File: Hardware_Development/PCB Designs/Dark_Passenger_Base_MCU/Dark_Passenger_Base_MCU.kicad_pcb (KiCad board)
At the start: 2 copper layers, 87.5 x 64.9 mm, 28 parts, among them J1 Conn_01x22, J10 SPARE I2C, J11 IMU, J12 Toggle Switches, J13 Spare, J14 Motor Encoder 1, J15 Motor Encoder 2, J16 RESET, J18 Motor Control, J2 Conn_01x22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

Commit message: Updates to Base PCB
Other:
- board text added: "Dark Passenger Base MCU REV: 1.0 Name: Ranil Ganlath Date: 03-28-2025 S/N:"
- board text removed: "Dark Passenger Base MCU REV: 1.0 Name: Ranil Ganlath Date: 03-27-2025 S/N:"
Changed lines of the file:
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@@
 	(title_block
 		(title "Dark Passenger Base MCU PCB")
-		(date "2025-03-27")
+		(date "2025-03-28")
 		(rev "1.0")
 		(company "Ranil Ganlath")
@@
 			(at -3.5558 -0.0508 0)
 			(layer "F.SilkS")
+			(hide yes)
 			(effects
 				(font
@@
 			(at -3.5558 0 0)
 			(layer "F.SilkS")
+			(hide yes)
 			(effects
 				(font
@@
 		)
 	)
+	(gr_text "5V"
+		(at 122.098 82.6516 90)
+		(layer "F.SilkS")
+		(effects
+			(font
+				(size 1 1)
+				(thickness 0.2)
+			)
+			(justify left bottom)
+		)
+	)
 	(gr_text "3V"
 		(at 85.892 54.6676 0)
@@
 		)
 	)
-	(gr_text "Dark Passenger \nBase MCU\nREV: 1.0\nName: Ranil Ganlath\nDate: 03-27-2025\n\nS/N:"
+	(gr_text "Dark Passenger \nBase MCU\nREV: 1.0\nName: Ranil Ganlath\nDate: 03-28-2025\n\nS/N:"
 		(at 100.508 94.58 0)
 		(layer "F.SilkS")
@@
 		)
 	)
+	(gr_text "GND"
+		(at 124.7904 83.7184 90)
+		(layer "F.SilkS")
+		(effects
+			(font
+				(size 1 1)
+				(thickness 0.2)
+			)
+			(justify left bottom)
+		)
+	)
 	(gr_text "Motor Encoder 3 / 4"
 		(at 97.5108 62.738 90)
@@
 	)
 	(gr_text "RST"
-		(at 113.462 63.5 0)
+		(at 113.208 66.294 0)
 		(layer "B.SilkS")
 		(effects
@@
 	)
 	(gr_text "GND"
-		(at 113.462 66.294 0)
+		(at 113.4112 63.5 0)
 		(layer "B.SilkS")
 		(effects
@@
 			)
 		)
+	)
+	(zone
+		(net 0)
+		(net_name "")
+		(layers "F.Cu" "B.Cu")
+		(hatch edge 0.5)
+		(connect_pads
+			(clearance 0)
+		)
+		(min_thickness 0.25)
+		(filled_areas_thickness no)
+		(keepout
+			(tracks allowed)
+			(vias allowed)
+			(pads allowed)
+			(copperpour not_allowed)
+			(footprints allowed)
+		)
+		(placement
+			(enabled no)
+			(sheetname "")
+		)
+		(fill
+			(thermal_gap 0.5)
+			(thermal_bridge_width 0.5)
+		)
+		(polygon
+			(pts
+				(xy 92.798023 91.137979) (xy 92.766261 90.815496) (xy 92.703043 90.497679) (xy 92.608979 90.18759)
+				(xy 92.484973 89.888213) (xy 92.33222 89.602433) (xy 92.152191 89.333001) (xy 91.946621 89.082512)
+				(xy 91.717488 88.853379) (xy 91.466999 88.647809) (xy 91.197567 88.46778) (xy 90.911787 88.315027)
+				(xy 90.61241 88.191021) (xy 90.302321 88.096957) (xy 89.984504 88.033739) (xy 89.662021 88.001977)
+				(xy 89.337979 88.001977) (xy 89.015496 88.033739) (xy 88.697679 88.096957) (xy 88.38759 88.191021)
+				(xy 88.088213 88.315027) (xy 87.802433 88.46778) (xy 87.533001 88.647809) (xy 87.282512 88.853379)
+				(xy 87.053379 89.082512) (xy 86.847809 89.333001) (xy 86.66778 89.602433) (xy 86.515027 89.888213)
+				(xy 86.391021 90.18759) (xy 86.296957 90.497679) (xy 86.233739 90.815496) (xy 86.201977 91.137979)
+				(xy 86.201977 91.462021) (xy 86.233739 91.784504) (xy 86.296957 92.102321) (xy 86.391021 92.41241)
+				(xy 86.515027 92.711787) (xy 86.66778 92.997567) (xy 86.847809 93.266999) (xy 87.053379 93.517488)
+				(xy 87.282512 93.746621) (xy 87.533001 93.952191) (xy 87.802433 94.13222) (xy 88.088213 94.284973)
+				(xy 88.38759 94.408979) (xy 88.697679 94.503043) (xy 89.015496 94.566261) (xy 89.337979 94.598023)
+				(xy 89.662021 94.598023) (xy 89.984504 94.566261) (xy 90.302321 94.503043) (xy 90.61241 94.408979)
+				(xy 90.911787 94.284973) (xy 91.197567 94.13222) (xy 91.466999 93.952191) (xy 91.717488 93.746621)
+				(xy 91.946621 93.517488) (xy 92.152191 93.266999) (xy 92.33222 92.997567) (xy 92.484973 92.711787)
+				(xy 92.608979 92.41241) (xy 92.703043 92.102321) (xy 92.766261 91.784504) (xy 92.798023 91.462021)
+			)
+		)
+	)
+	(zone
+		(net 0)
+		(net_name "")
+		(layers "F.Cu" "B.Cu")
+		(hatch edge 0.5)
+		(connect_pads
+			(clearance 0)
+		)
+		(min_thickness 0.25)
+		(filled_areas_thickness no)
+		(keepout
+			(tracks allowed)
+			(vias allowed)
+			(pads allowed)
+			(copperpour not_allowed)
+			(footprints allowed)
+		)
+		(placement
+			(enabled no)
+			(sheetname "")
+		)
+		(fill
+			(thermal_gap 0.5)
+			(thermal_bridge_width 0.5)
+		)
+		(polygon
+			(pts
+				(xy 171.538023 91.137979) (xy 171.506261 90.815496) (xy 171.443043 90.497679) (xy 171.348979 90.18759)
+				(xy 171.224973 89.888213) (xy 171.07222 89.602433) (xy 170.892191 89.333001) (xy 170.686621 89.082512)
+				(xy 170.457488 88.853379) (xy 170.206999 88.647809) (xy 169.937567 88.46778) (xy 169.651787 88.315027)
+				(xy 169.35241 88.191021) (xy 169.042321 88.096957) (xy 168.724504 88.033739) (xy 168.402021 88.001977)
+				(xy 168.077979 88.001977) (xy 167.755496 88.033739) (xy 167.437679 88.096957) (xy 167.12759 88.191021)
+				(xy 166.828213 88.315027) (xy 166.542433 88.46778) (xy 166.273001 88.647809) (xy 166.022512 88.853379)
+				(xy 165.793379 89.082512) (xy 165.587809 89.333001) (xy 165.40778 89.602433) (xy 165.255027 89.888213)
+				(xy 165.131021 90.18759) (xy 165.036957 90.497679) (xy 164.973739 90.815496) (xy 164.941977 91.137979)
+				(xy 164.941977 91.462021) (xy 164.973739 91.784504) (xy 165.036957 92.102321) (xy 165.131021 92.41241)
+				(xy 165.255027 92.711787) (xy 165.40778 92.997567) (xy 165.587809 93.266999) (xy 165.793379 93.517488)
+				(xy 166.022512 93.746621) (xy 166.273001 93.952191) (xy 166.542433 94.13222) (xy 166.828213 94.284973)
+				(xy 167.12759 94.408979) (xy 167.437679 94.503043) (xy 167.755496 94.566261) (xy 168.077979 94.598023)
+				(xy 168.402021 94.598023) (xy 168.724504 94.566261) (xy 169.042321 94.503043) (xy 169.35241 94.408979)
+				(xy 169.651787 94.284973) (xy 169.937567 94.13222) (xy 170.206999 93.952191) (xy 170.457488 93.746621)
+				(xy 170.686621 93.517488) (xy 170.892191 93.266999) (xy 171.07222 92.997567) (xy 171.224973 92.711787)
+				(xy 171.348979 92.41241) (xy 171.443043 92.102321) (xy 171.506261 91.784504) (xy 171.538023 91.462021)
+			)
+		)
+	)
+	(zone
+		(net 0)
+		(net_name "")
+		(layers "F.Cu" "B.Cu")
+		(hatch edge 0.5)
+		(connect_pads
+			(clearance 0)
+		)
+		(min_thickness 0.25)
+		(filled_areas_thickness no)
+		(keepout
+			(tracks allowed)
+			(vias allowed)
+			(pads allowed)
+			(copperpour not_allowed)
+			(footprints allowed)
+		)
+		(placement
+			(enabled no)
+			(sheetname "")
+		)
+		(fill
+			(thermal_gap 0.5)
+			(thermal_bridge_width 0.5)
+		)
+		(polygon
+			(pts
+				(xy 171.547823 35.245579) (xy 171.516061 34.923096) (xy 171.452843 34.605279) (xy 171.358779 34.29519)
+				(xy 171.234773 33.995813) (xy 171.08202 33.710033) (xy 170.901991 33.440601) (xy 170.696421 33.190112)
+				(xy 170.467288 32.960979) (xy 170.216799 32.755409) (xy 169.947367 32.57538) (xy 169.661587 32.422627)
+				(xy 169.36221 32.298621) (xy 169.052121 32.204557) (xy 168.734304 32.141339) (xy 168.411821 32.109577)
+				(xy 168.087779 32.109577) (xy 167.765296 32.141339) (xy 167.447479 32.204557) (xy 167.13739 32.298621)
+				(xy 166.838013 32.422627) (xy 166.552233 32.57538) (xy 166.282801 32.755409) (xy 166.032312 32.960979)
+				(xy 165.803179 33.190112) (xy 165.597609 33.440601) (xy 165.41758 33.710033) (xy 165.264827 33.995813)
+				(xy 165.140821 34.29519) (xy 165.046757 34.605279) (xy 164.983539 34.923096) (xy 164.951777 35.245579)
+				(xy 164.951777 35.569621) (xy 164.983539 35.892104) (xy 165.046757 36.209921) (xy 165.140821 36.52001)
+				(xy 165.264827 36.819387) (xy 165.41758 37.105167) (xy 165.597609 37.374599) (xy 165.803179 37.625088)
+				(xy 166.032312 37.854221) (xy 166.282801 38.059791) (xy 166.552233 38.23982) (xy 166.838013 38.392573)
+				(xy 167.13739 38.516579) (xy 167.447479 38.610643) (xy 167.765296 38.673861) (xy 168.087779 38.705623)
+				(xy 168.411821 38.705623) (xy 168.734304 38.673861) (xy 169.052121 38.610643) (xy 169.36221 38.516579)
+				(xy 169.661587 38.392573) (xy 169.947367 38.23982) (xy 170.216799 38.059791) (xy 170.467288 37.854221)
+				(xy 170.696421 37.625088) (xy 170.901991 37.374599) (xy 171.08202 37.105167) (xy 171.234773 36.819387)
+				(xy 171.358779 36.52001) (xy 171.452843 36.209921) (xy 171.516061 35.892104) (xy 171.547823 35.569621)
+			)
+		)
+	)
+	(zone
+		(net 0)
+		(net_name "")
+		(layers "F.Cu" "B.Cu")
+		(hatch edge 0.5)
+		(connect_pads
+			(clearance 0)
+		)
+		(min_thickness 0.25)
+		(filled_areas_thickness no)
+		(keepout
+			(tracks allowed)
+			(vias allowed)
+			(pads allowed)
+			(copperpour not_allowed)
+			(footprints allowed)
+		)
+		(placement
+			(enabled no)
+			(sheetname "")
+		)
+		(fill
+			(thermal_gap 0.5)
+			(thermal_bridge_width 0.5)
+		)
+		(polygon
+			(pts
+				(xy 92.798023 35.257979) (xy 92.766261 34.935496) (xy 92.703043 34.617679) (xy 92.608979 34.30759)
+				(xy 92.484973 34.008213) (xy 92.33222 33.722433) (xy 92.152191 33.453001) (xy 91.946621 33.202512)
+				(xy 91.717488 32.973379) (xy 91.466999 32.767809) (xy 91.197567 32.58778) (xy 90.911787 32.435027)
+				(xy 90.61241 32.311021) (xy 90.302321 32.216957) (xy 89.984504 32.153739) (xy 89.662021 32.121977)
+				(xy 89.337979 32.121977) (xy 89.015496 32.153739) (xy 88.697679 32.216957) (xy 88.38759 32.311021)
+				(xy 88.088213 32.435027) (xy 87.802433 32.58778) (xy 87.533001 32.767809) (xy 87.282512 32.973379)
+				(xy 87.053379 33.202512) (xy 86.847809 33.453001) (xy 86.66778 33.722433) (xy 86.515027 34.008213)
+				(xy 86.391021 34.30759) (xy 86.296957 34.617679) (xy 86.233739 34.935496) (xy 86.201977 35.257979)
+				(xy 86.201977 35.582021) (xy 86.233739 35.904504) (xy 86.296957 36.222321) (xy 86.391021 36.53241)
+				(xy 86.515027 36.831787) (xy 86.66778 37.117567) (xy 86.847809 37.386999) (xy 87.053379 37.637488)
+				(xy 87.282512 37.866621) (xy 87.533001 38.072191) (xy 87.802433 38.25222) (xy 88.088213 38.404973)
+				(xy 88.38759 38.528979) (xy 88.697679 38.623043) (xy 89.015496 38.686261) (xy 89.337979 38.718023)
+				(xy 89.662021 38.718023) (xy 89.984504 38.686261) (xy 90.302321 38.623043) (xy 90.61241 38.528979)
+				(xy 90.911787 38.404973) (xy 91.197567 38.25222) (xy 91.466999 38.072191) (xy 91.717488 37.866621)
+				(xy 91.946621 37.637488) (xy 92.152191 37.386999) (xy 92.33222 37.117567) (xy 92.484973 36.831787)
+				(xy 92.608979 36.53241) (xy 92.703043 36.222321) (xy 92.766261 35.904504) (xy 92.798023 35.582021)
+			)
+		)

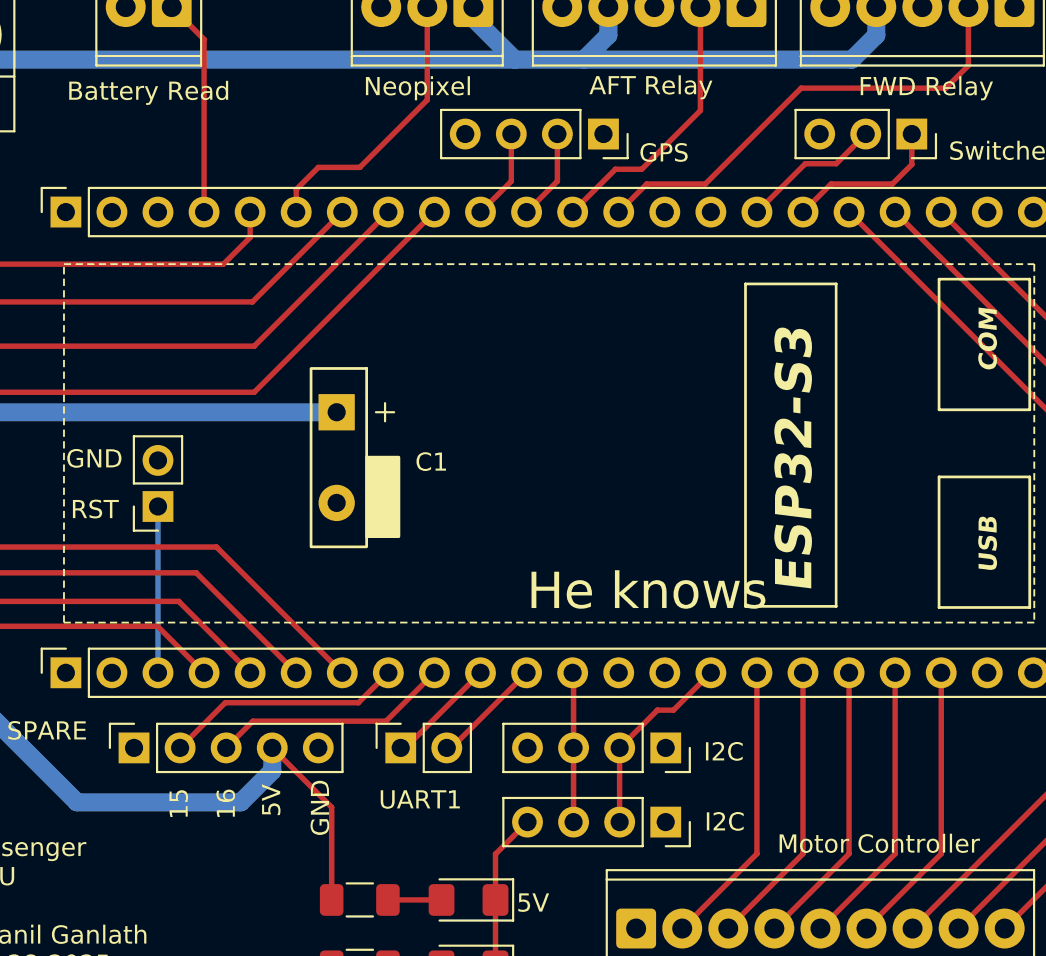
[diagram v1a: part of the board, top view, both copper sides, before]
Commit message: Updates to code based on new pinouts from PCBs
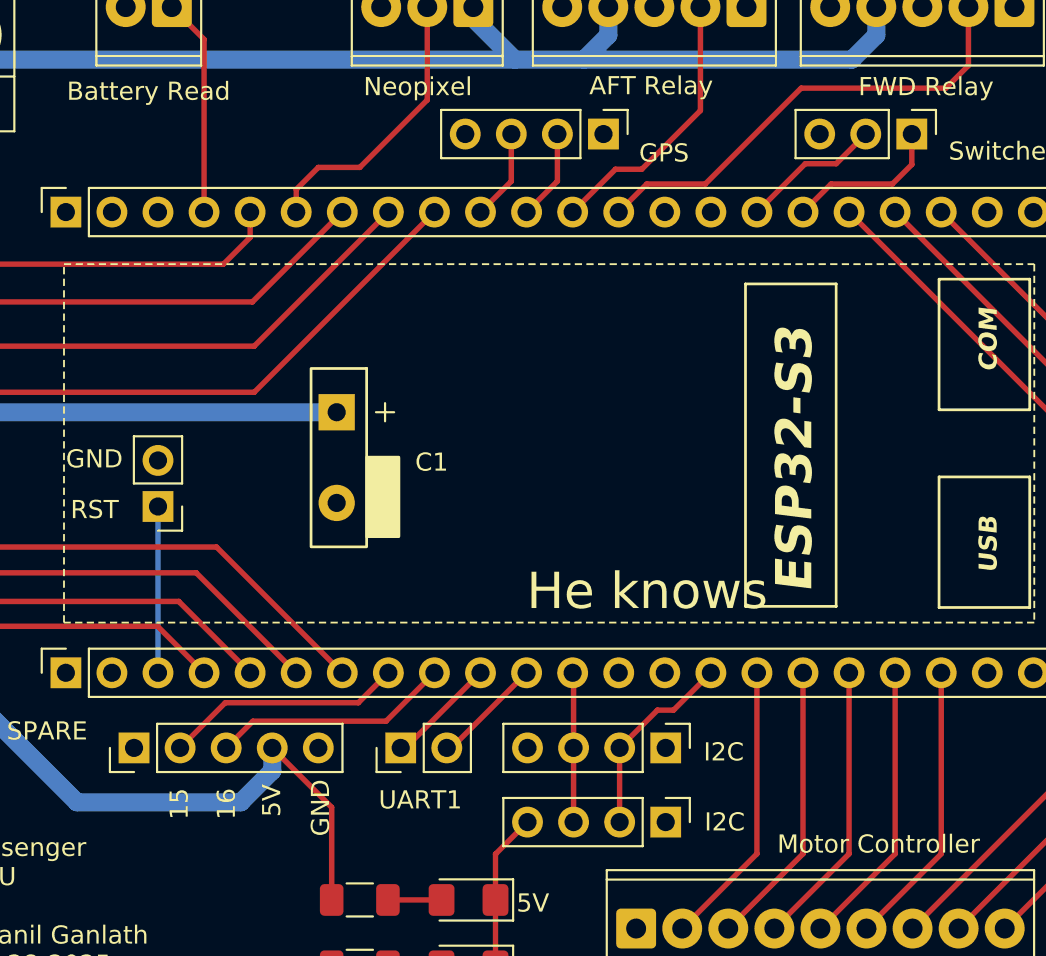
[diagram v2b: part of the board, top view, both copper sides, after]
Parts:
- J10, J11, J8: footprint Connector_PinSocket_2.54mm:PinSocket_1x04_P2.54mm_Vertical -> GanlathLib:BlankPin_1x04_P2.54mm
- J12: footprint Connector_PinSocket_2.54mm:PinSocket_1x03_P2.54mm_Vertical -> GanlathLib:BlankPin_1x03_P2.54mm
- J13: footprint Connector_PinSocket_2.54mm:PinSocket_1x05_P2.54mm_Vertical -> GanlathLib:BlankPin_1x05_P2.54mm
- J16, J9: footprint Connector_PinSocket_2.54mm:PinSocket_1x02_P2.54mm_Vertical -> GanlathLib:BlankPin_1x02_P2.54mm
